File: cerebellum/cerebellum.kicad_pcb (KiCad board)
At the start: 4 copper layers, 91.5 x 52 mm, 79 parts, among them J1 PWR_OUT, J2 PWR_IN, J3 Conn_01x04, J4 gh1.25, 3p, J5 DF40C-100DS-0.4V(51), J6 DF40C-100DS-0.4V(51), Q1 AP2300, U1 GD32F405VGHx, U2 TPS5430DDAR, U3 BMI088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

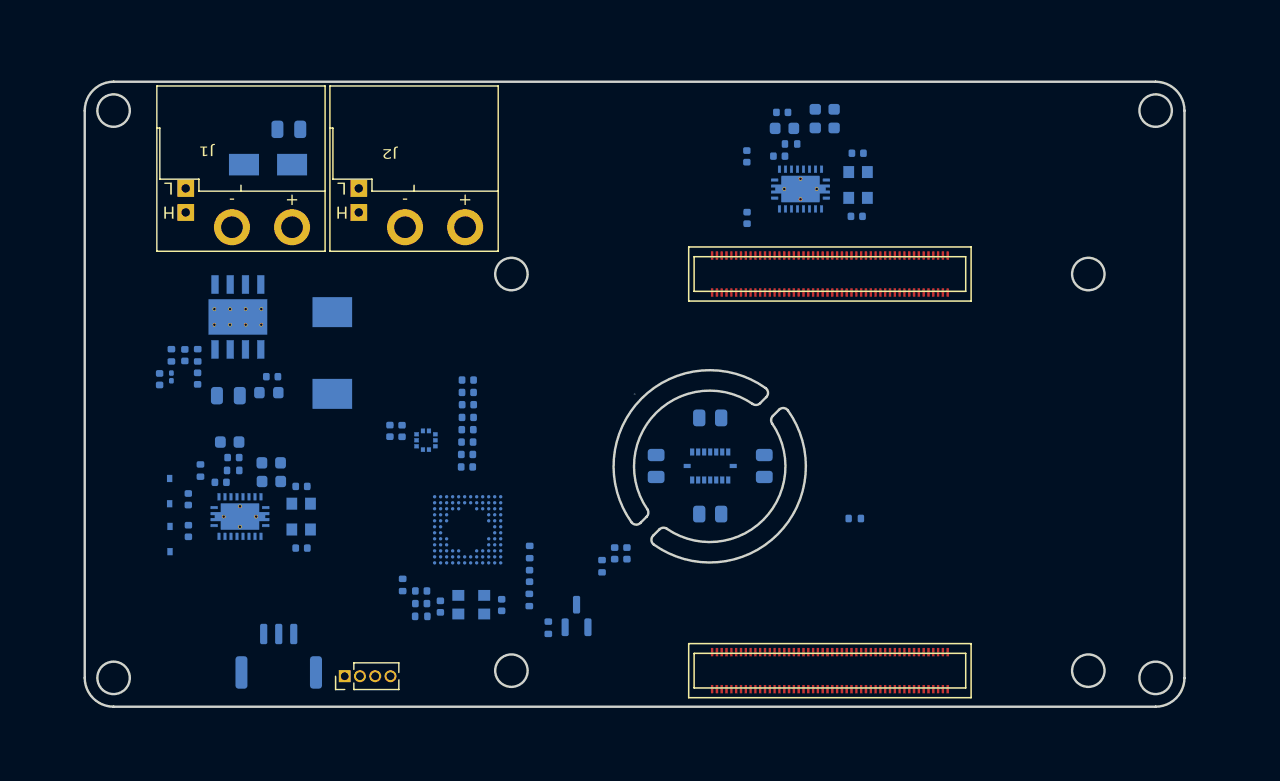
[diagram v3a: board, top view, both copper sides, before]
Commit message: [New] Complete cerebellum
* Refactor cerebellum, now cerebellum includes features of heart &
  cerebellum

Signed-off-by: Homalozoa <nx.tardis@gmail.com>
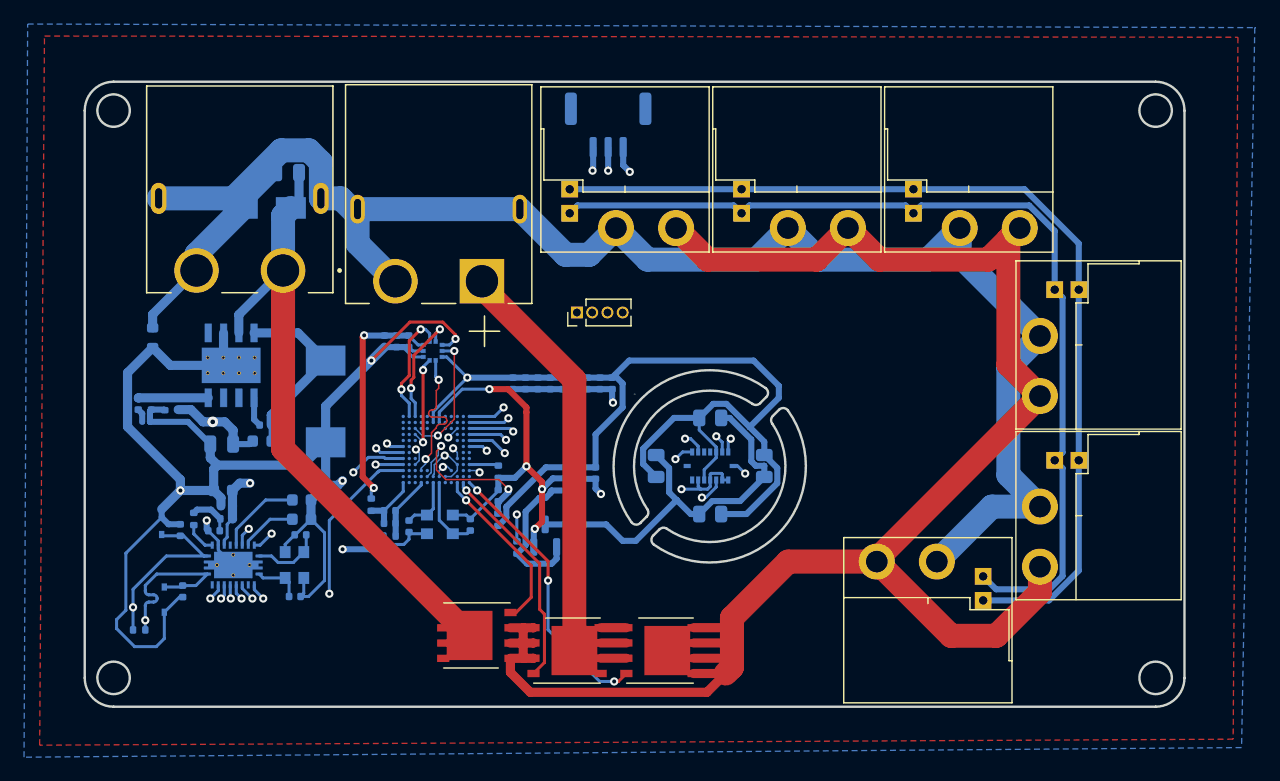
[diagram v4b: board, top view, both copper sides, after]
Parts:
- removed C34: 10pF, 10%, 50V, Capacitor_SMD:C_0402_1005Metric
- removed C35: 10nF, 10%, 50V, Capacitor_SMD:C_0402_1005Metric
- removed C36: 470nF, 10%, 50V, Capacitor_SMD:C_0603_1608Metric
- removed C37, C38: 100pF, 10%, 10V, Capacitor_SMD:C_0402_1005Metric
- removed C39: 100nF, 10%, 50V, Capacitor_SMD:C_0402_1005Metric
- removed C40, C41: 10uF, 10%, 50V, Capacitor_SMD:C_0603_1608Metric
- removed J6: DF40C-100DS-0.4V(51), Rolling_Custom:HRS_DF40C-100DS-0.4V(51)
- removed R16: 3k, Resistor_SMD:R_0402_1005Metric
- removed U7: TCAN4550RGYRQ1, Rolling_Custom:VQFN20
- removed Y3: 40M, Oscillator:Oscillator_SMD_EuroQuartz_XO32-4Pin_3.2x2.5mm
- added C51: 100nF, 10%, 10V, Capacitor_SMD:C_0402_1005Metric, B.Cu at (129.2, 95.6)
- added FB1: 220R, Resistor_SMD:R_0603_1608Metric, B.Cu at (109.9, 95.3)
- added J10: Arm_R, Rolling_Custom:XT30PW(2+2), F.Cu at (163.5, 86.2)
- added J11: Light, Rolling_Custom:XT30PW(2+2), F.Cu at (174.4, 113.9)
- added J7: Leg_L, Rolling_Custom:XT30PW(2+2), F.Cu at (177.8, 86.2)
- added J8: Leg_R, Rolling_Custom:XT30PW(2+2), F.Cu at (183.7, 95.9)
- added J9: Arm_L, Rolling_Custom:XT30PW(2+2), F.Cu at (183.7, 110.1)
- added Q2: FH1404G6, Rolling_Custom:PDFN5X6-8L, F.Cu at (136.8, 119.9)
- added Q3: FH1404G6, Rolling_Custom:PDFN5X6-8L, F.Cu at (144.4, 121.5)
- added Q4: FH1404G6, Rolling_Custom:PDFN5X6-8L, F.Cu at (152.2, 121.5)
- C14, C15: value 10pF, 10%, 50V -> 8.2pF, 10%, 50V
- C33: value 10pF, 10%, 50V -> 10uF, 10%, 10V
- J1: value PWR_OUT -> Power_IN; footprint Rolling_Custom:XT30PW(2+2) -> Rolling_Custom:AMASS_XT60PW-F
- J2: value PWR_IN -> Power_Back; footprint Rolling_Custom:XT30PW(2+2) -> Rolling_Custom:AMASS_XT60PW-M
- J3: value Conn_01x04 -> GD_LINK
- J4: value gh1.25, 3p -> GD_LINK
- J5: value DF40C-100DS-0.4V(51) -> Head; footprint Rolling_Custom:HRS_DF40C-100DS-0.4V(51) -> Rolling_Custom:XT30PW(2+2)
- R8: value 33k -> 120R
- U1: footprint Package_BGA:UFBGA-100_7x7mm_Layout12x12_P0.5mm -> Rolling_Custom:Modified-BGA-100_7x7mm_Layout12x12_P0.5mm
- moved R8 60.3 mm to (108.8, 119.6), turned to 0 degrees
- moved J4 52.0 mm to (147.8, 77.6), turned to 0 degrees
- moved J5 40.6 mm to (149.2, 86.2), turned to 180 degrees
- moved J3 35.9 mm to (145.2, 93.2)
- moved C33 24.6 mm to (148.1, 99.1), turned to -90 degrees
- moved C9 11.0 mm to (147.1, 99.1), turned to 90 degrees
- moved C10 9.99 mm to (146.1, 99.1), turned to 90 degrees
- moved C7 9.10 mm to (145.1, 99.1), turned to -90 degrees
- moved C8 8.37 mm to (144.0, 99.1), turned to -90 degrees
- moved C4 7.94 mm to (139.9, 99.1), turned to -90 degrees
- moved C20 7.88 mm to (143.0, 99.1), turned to -90 degrees
- moved C5 7.65 mm to (140.9, 99.1), turned to -90 degrees
- moved C6 7.63 mm to (141.9, 99.1), turned to -90 degrees
- moved C31 7.48 mm to (131.2, 95.6)
- moved C32 7.47 mm to (130.2, 95.6)
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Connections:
- C13 pad 2: GND -> GNDA
- C33 pad 1: GND -> +3V3
- C33 pad 2: TCANPi_OSC_IN -> GND
- D1 pad 1: GND -> GNDA
- J1 pad 2: GND -> GNDA
- J2 pad 1: +24V -> EXT_PWR
- J2 pad 2: GND -> GNDA
- J5 pad 1: unconnected-(J5-Pad1) -> PWR_EXPORT
- J5 pad 2: unconnected-(J5-Pad2) -> GNDA
- J5 pad 3: unconnected-(J5-Pad3) -> CAN_H
- J5 pad 4: unconnected-(J5-Pad4) -> CAN_L
- R8 pad 1: TCANPi_WAKE -> CAN_H
- R8 pad 2: Net-(C35-Pad2) -> CAN_L
- U1 pad A1: unconnected-(U1-PadA1) -> PWRCT_3
- U1 pad A12: GYRO_SCS -> ACC_SCS
- U1 pad A3: unconnected-(U1-PadA3) -> BMI_HEAT
- U1 pad A9: ACC_SCS -> GYRO_SCS
- U1 pad B1: unconnected-(U1-PadB1) -> PWRCT_2
- U1 pad B7: BMI_INT4 -> unconnected-(U1-PadB7)
- U1 pad C1: unconnected-(U1-PadC1) -> PWRCT_1
- U1 pad C8: BMI_INT3 -> unconnected-(U1-PadC8)
- U1 pad D10: BMI_INT2 -> unconnected-(U1-PadD10)
- U1 pad E10: BMI_INT1 -> unconnected-(U1-PadE10)
- U1 pad H10: BMI_HEAT -> unconnected-(U1-PadH10)
- U3 pad 1: BMI_INT2 -> unconnected-(U3-Pad1)
- U3 pad 12: BMI_INT3 -> unconnected-(U3-Pad12)
- U3 pad 13: BMI_INT4 -> unconnected-(U3-Pad13)
- U3 pad 16: BMI_INT1 -> unconnected-(U3-Pad16)
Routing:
- net GND: track 0.00 -> 253.0 mm, vias 0 -> 15
- net +3V3: track 0.00 -> 182.6 mm, vias 0 -> 6
- net CAN_L: track 0.00 -> 167.0 mm, vias 0 -> 1
- net CAN_H: track 0.00 -> 166.4 mm, vias 0 -> 1
- net PWR_EXPORT: track 0.00 -> 145.5 mm
- net GNDA: track 0.00 -> 142.9 mm
- net +24V: track 0.00 -> 77.6 mm, vias 0 -> 1
- net BMI_SDO: track 0.00 -> 48.7 mm, vias 0 -> 3
- net BMI_SDI: track 0.00 -> 42.8 mm, vias 0 -> 2
- net EXT_PWR: track 0.00 -> 40.4 mm
- net Net-(Q1-Pad3): track 0.00 -> 33.6 mm
- net TCAN_SDO: track 0.00 -> 33.6 mm, vias 0 -> 2
- net SWCLK: track 0.00 -> 32.8 mm, vias 0 -> 2
- net ACC_SCS: track 0.00 -> 30.3 mm, vias 0 -> 2
- net BMI_SCK: track 0.00 -> 29.7 mm, vias 0 -> 2
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- added copper zone on In2.Cu, net +3V3
- added copper zone on In1.Cu, net EXT_PWR
- added copper zone on B.Cu, net GND
- added copper zone on F.Cu, net GNDA
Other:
- outline, holes or cut-outs redrawn

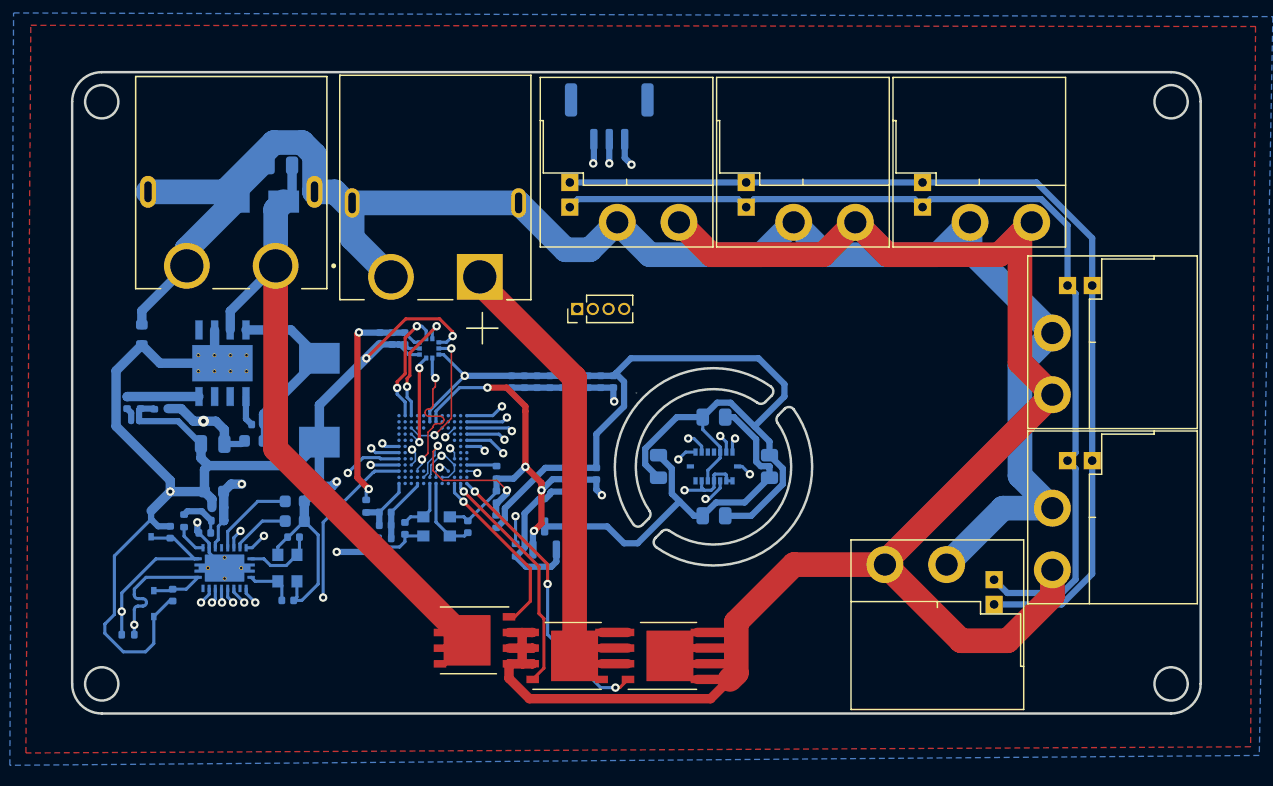
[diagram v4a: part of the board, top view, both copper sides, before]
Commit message: [New] Change mounting hole in cerebellum
Signed-off-by: Homalozoa <nx.tardis@gmail.com>
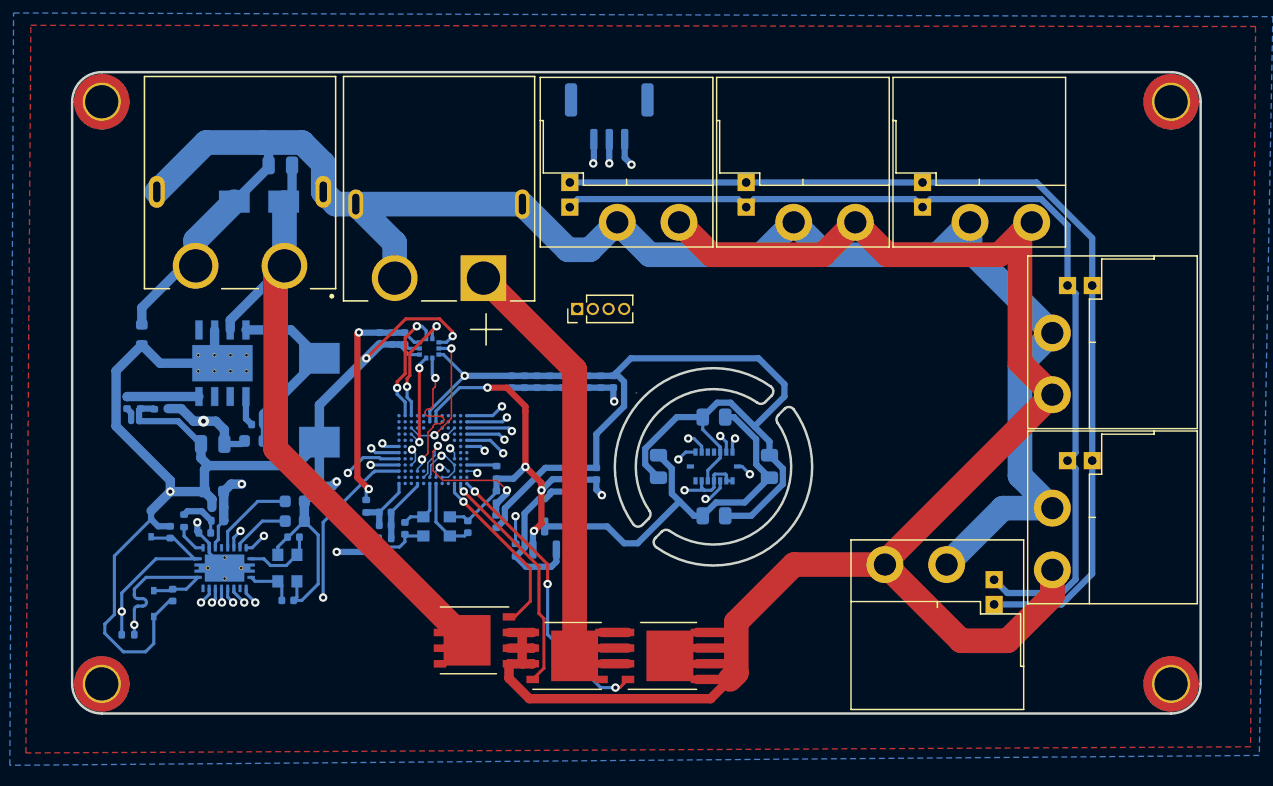
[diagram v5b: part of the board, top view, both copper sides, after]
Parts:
- added Mount1: MountingHole_2.7mm_M2.5_ISO7380_Pad_TopBottom, MountingHole:MountingHole_2.7mm_M2.5_ISO7380_Pad_TopBottom, F.Cu at (106.7, 76.4)
- added Mount2: MountingHole_2.7mm_M2.5_ISO7380_Pad_TopBottom, MountingHole:MountingHole_2.7mm_M2.5_ISO7380_Pad_TopBottom, F.Cu at (193.3, 76.4)
- added Mount3: MountingHole_2.7mm_M2.5_ISO7380_Pad_TopBottom, MountingHole:MountingHole_2.7mm_M2.5_ISO7380_Pad_TopBottom, F.Cu at (193.3, 123.6)
- added Mount4: MountingHole_2.7mm_M2.5_ISO7380_Pad_TopBottom, MountingHole:MountingHole_2.7mm_M2.5_ISO7380_Pad_TopBottom, F.Cu at (106.7, 123.6)
- moved J1 0.71 mm to (117.9, 89.7)
- moved J2 0.32 mm to (134.0, 84.7)
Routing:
- net +24V: track 77.6 -> 78.2 mm
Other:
- outline, holes or cut-outs redrawn

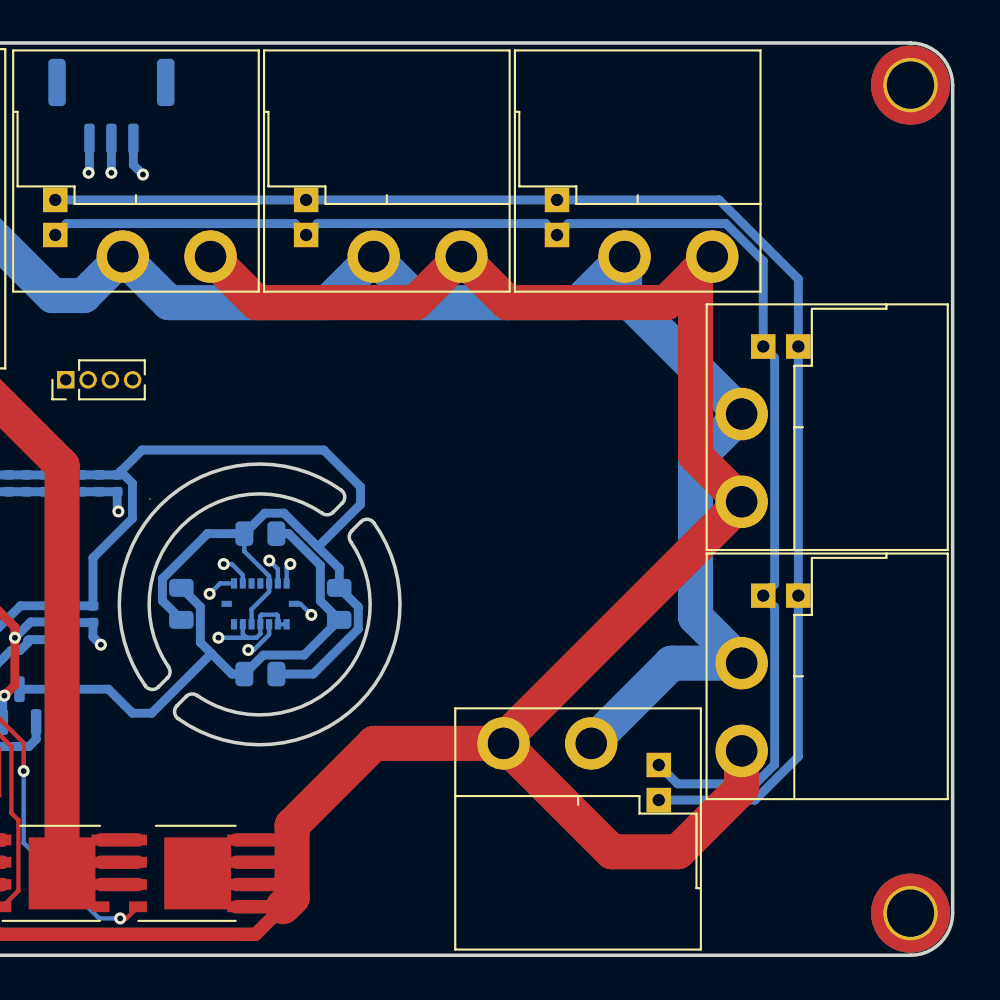
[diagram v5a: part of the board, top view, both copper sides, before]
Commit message: [New] Add some capacities to cerebellum
Signed-off-by: Homalozoa <nx.tardis@gmail.com>
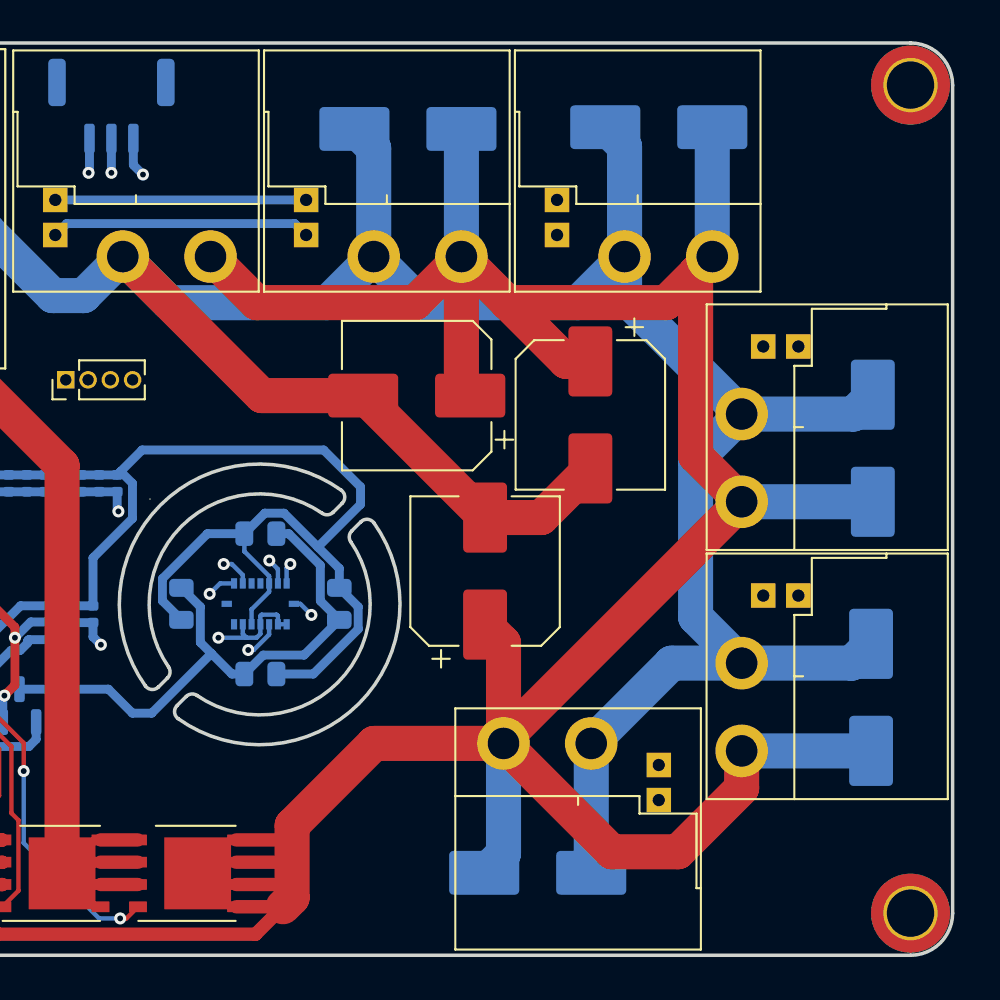
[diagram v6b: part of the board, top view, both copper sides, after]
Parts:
- added C34: 47uf, Capacitor_SMD:CP_Elec_8x6.2, B.Cu at (172.1, 121.3)
- added C35: 47uf, Capacitor_SMD:CP_Elec_8x6.2, B.Cu at (191.1, 111.3)
- added C36: 47uf, Capacitor_SMD:CP_Elec_8x6.2, F.Cu at (165.2, 94.1)
- added C37: 47uf, Capacitor_SMD:CP_Elec_8x6.2, B.Cu at (191.2, 97.1)
- added C38: 47uf, Capacitor_SMD:CP_Elec_8x6.2, F.Cu at (175.1, 95.2)
- added C39: 47uf, Capacitor_SMD:CP_Elec_8x6.2, B.Cu at (164.7, 78.9)
- added C40: 47uf, Capacitor_SMD:CP_Elec_8x6.2, F.Cu at (169.1, 104.1)
- added C41: 47uf, Capacitor_SMD:CP_Elec_8x6.2, B.Cu at (179.0, 78.8)
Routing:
- net GNDA: track 142.8 -> 215.5 mm
- net PWR_EXPORT: track 145.5 -> 204.3 mm
